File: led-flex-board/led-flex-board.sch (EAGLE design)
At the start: 30 parts

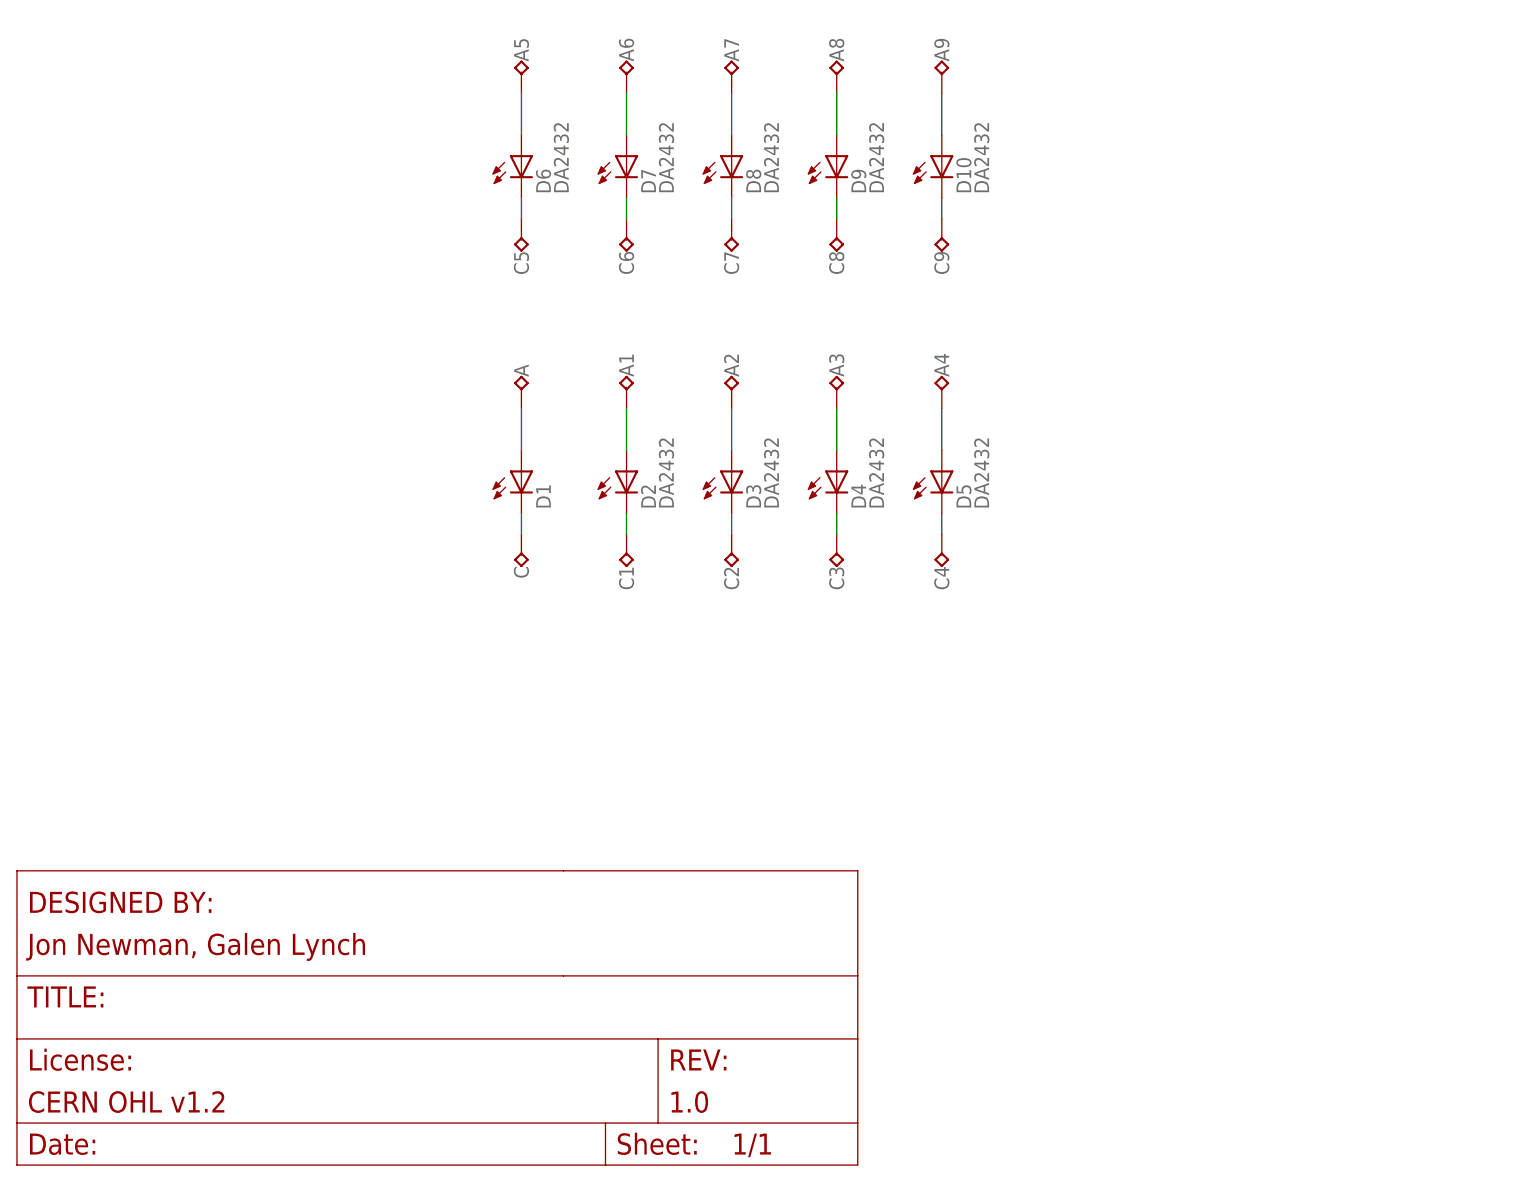
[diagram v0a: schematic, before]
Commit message: Added more designs to led-flex-board
- Multiple lead length options
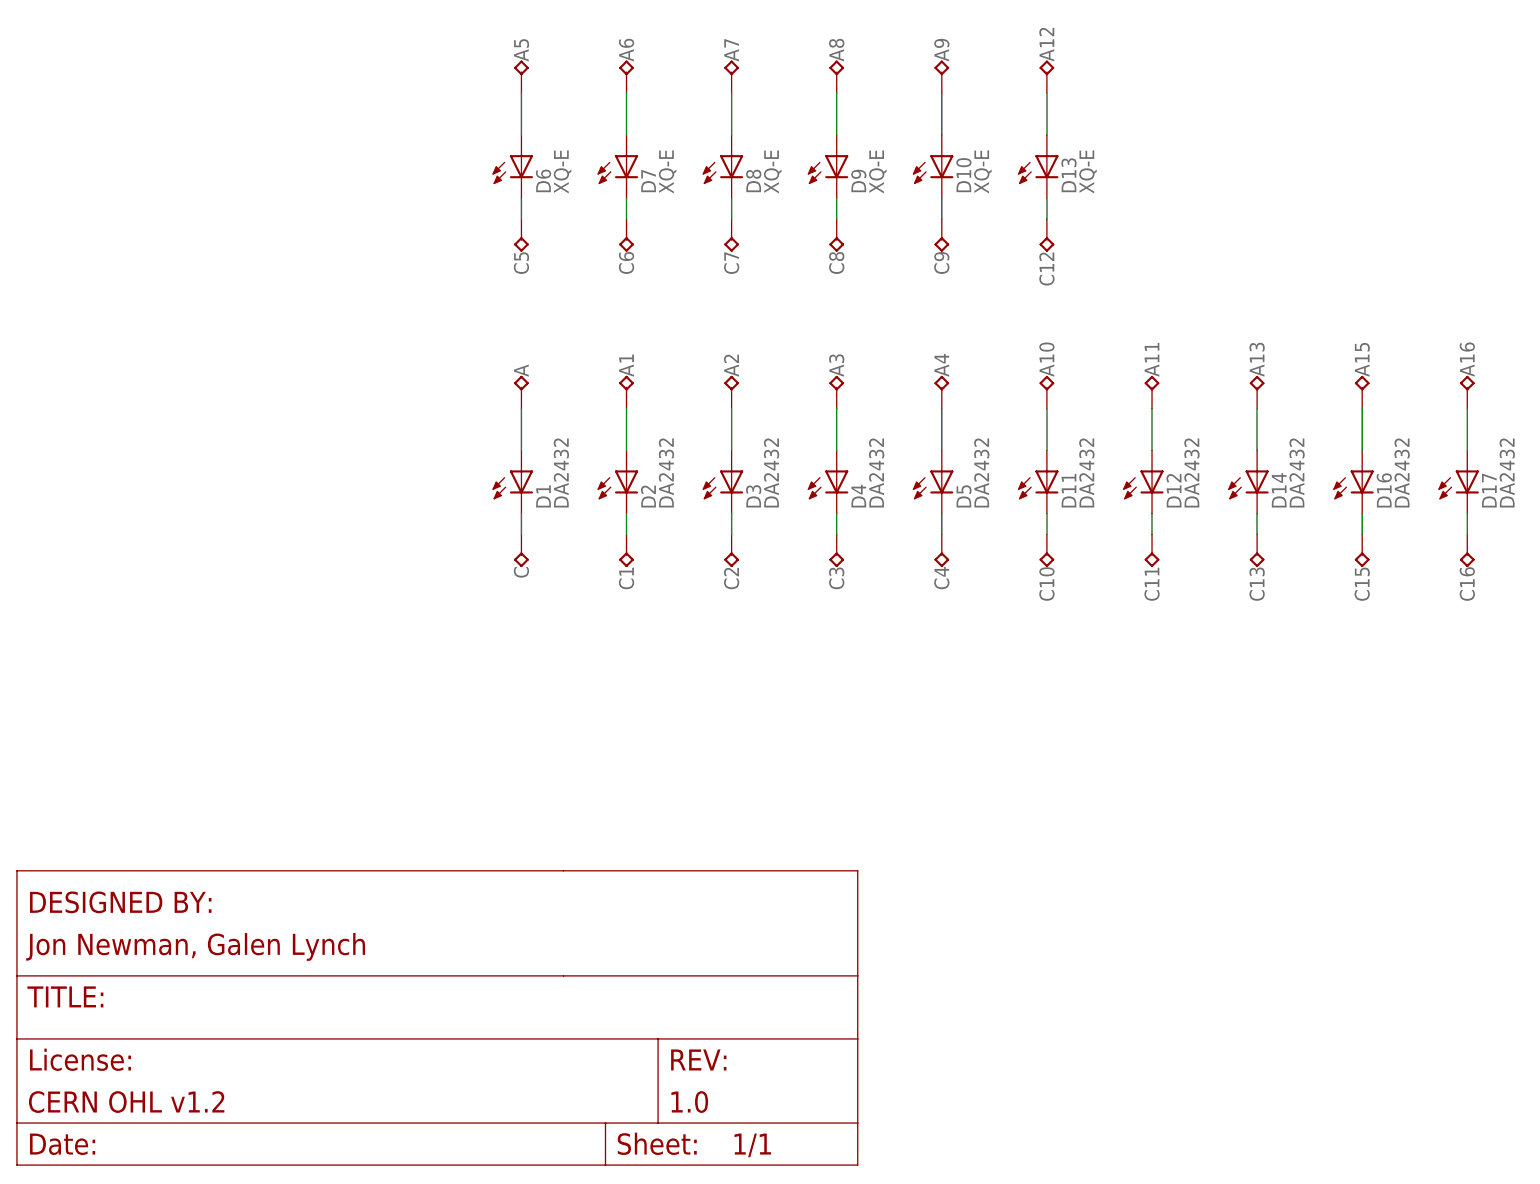
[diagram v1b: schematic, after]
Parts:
- added A10, A11, A12, A13, A15, A16, C10, C11, C12, C13, C15, C16: (no value), jonnew:TP_S0.6X1.5MM
- added D11, D12, D14, D16, D17: DA2432, jonnew:LED_DA2432
- added D13: XQ-E, jonnew:LED_XLAMP1.6X1.6MM
- D1: value (none) -> DA2432
- D10, D6, D7, D8, D9: value DA2432 -> XQ-E
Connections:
- new net N$21: C10.TP, D11.C
- new net N$22: A10.TP, D11.A
- new net N$23: C11.TP, D12.C
- new net N$24: A11.TP, D12.A
- new net N$25: C12.TP, D13.C
- new net N$26: A12.TP, D13.A
- new net N$27: C13.TP, D14.C
- new net N$28: A13.TP, D14.A
- new net N$31: C15.TP, D16.C
- new net N$32: A15.TP, D16.A
- new net N$33: C16.TP, D17.C
- new net N$34: A16.TP, D17.A
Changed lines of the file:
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@@
 </classes>
 <parts>
-<part name="D1" library="jonnew" deviceset="LED" device="_DA2432"/>
+<part name="D1" library="jonnew" deviceset="LED" device="_DA2432" value="DA2432"/>
 <part name="A" library="jonnew" deviceset="TP" device="_S0.6X1.5MM"/>
 <part name="C" library="jonnew" deviceset="TP" device="_S0.6X1.5MM"/>
@@
 <part name="A4" library="jonnew" deviceset="TP" device="_S0.6X1.5MM"/>
 <part name="C4" library="jonnew" deviceset="TP" device="_S0.6X1.5MM"/>
-<part name="D6" library="jonnew" deviceset="LED" device="_XLAMP1.6X1.6MM" value="DA2432"/>
+<part name="D6" library="jonnew" deviceset="LED" device="_XLAMP1.6X1.6MM" value="XQ-E"/>
 <part name="A5" library="jonnew" deviceset="TP" device="_S0.6X1.5MM"/>
 <part name="C5" library="jonnew" deviceset="TP" device="_S0.6X1.5MM"/>
-<part name="D7" library="jonnew" deviceset="LED" device="_XLAMP1.6X1.6MM" value="DA2432"/>
+<part name="D7" library="jonnew" deviceset="LED" device="_XLAMP1.6X1.6MM" value="XQ-E"/>
 <part name="A6" library="jonnew" deviceset="TP" device="_S0.6X1.5MM"/>
 <part name="C6" library="jonnew" deviceset="TP" device="_S0.6X1.5MM"/>
-<part name="D8" library="jonnew" deviceset="LED" device="_XLAMP1.6X1.6MM" value="DA2432"/>
+<part name="D8" library="jonnew" deviceset="LED" device="_XLAMP1.6X1.6MM" value="XQ-E"/>
 <part name="A7" library="jonnew" deviceset="TP" device="_S0.6X1.5MM"/>
 <part name="C7" library="jonnew" deviceset="TP" device="_S0.6X1.5MM"/>
-<part name="D9" library="jonnew" deviceset="LED" device="_XLAMP1.6X1.6MM" value="DA2432"/>
+<part name="D9" library="jonnew" deviceset="LED" device="_XLAMP1.6X1.6MM" value="XQ-E"/>
 <part name="A8" library="jonnew" deviceset="TP" device="_S0.6X1.5MM"/>
 <part name="C8" library="jonnew" deviceset="TP" device="_S0.6X1.5MM"/>
-<part name="D10" library="jonnew" deviceset="LED" device="_XLAMP1.6X1.6MM" value="DA2432"/>
+<part name="D10" library="jonnew" deviceset="LED" device="_XLAMP1.6X1.6MM" value="XQ-E"/>
 <part name="A9" library="jonnew" deviceset="TP" device="_S0.6X1.5MM"/>
 <part name="C9" library="jonnew" deviceset="TP" device="_S0.6X1.5MM"/>
 <part name="U$1" library="jonnew" deviceset="DOCFIELD-GEN" device=""/>
+<part name="D11" library="jonnew" deviceset="LED" device="_DA2432" value="DA2432"/>
+<part name="A10" library="jonnew" deviceset="TP" device="_S0.6X1.5MM"/>
+<part name="C10" library="jonnew" deviceset="TP" device="_S0.6X1.5MM"/>
+<part name="D12" library="jonnew" deviceset="LED" device="_DA2432" value="DA2432"/>
+<part name="A11" library="jonnew" deviceset="TP" device="_S0.6X1.5MM"/>
+<part name="C11" library="jonnew" deviceset="TP" device="_S0.6X1.5MM"/>
+<part name="D13" library="jonnew" deviceset="LED" device="_XLAMP1.6X1.6MM" value="XQ-E"/>
+<part name="A12" library="jonnew" deviceset="TP" device="_S0.6X1.5MM"/>
+<part name="C12" library="jonnew" deviceset="TP" device="_S0.6X1.5MM"/>
+<part name="D14" library="jonnew" deviceset="LED" device="_DA2432" value="DA2432"/>
+<part name="A13" library="jonnew" deviceset="TP" device="_S0.6X1.5MM"/>
+<part name="C13" library="jonnew" deviceset="TP" device="_S0.6X1.5MM"/>
+<part name="D16" library="jonnew" deviceset="LED" device="_DA2432" value="DA2432"/>
+<part name="A15" library="jonnew" deviceset="TP" device="_S0.6X1.5MM"/>
+<part name="C15" library="jonnew" deviceset="TP" device="_S0.6X1.5MM"/>
+<part name="D17" library="jonnew" deviceset="LED" device="_DA2432" value="DA2432"/>
+<part name="A16" library="jonnew" deviceset="TP" device="_S0.6X1.5MM"/>
+<part name="C16" library="jonnew" deviceset="TP" device="_S0.6X1.5MM"/>
 </parts>
 <sheets>
@@
 <instance part="C9" gate="G$1" x="121.92" y="119.38" rot="R180"/>
 <instance part="U$1" gate="G$1" x="10.16" y="7.62"/>
+<instance part="D11" gate="G$1" x="134.62" y="91.44"/>
+<instance part="A10" gate="G$1" x="134.62" y="101.6"/>
+<instance part="C10" gate="G$1" x="134.62" y="81.28" rot="R180"/>
+<instance part="D12" gate="G$1" x="147.32" y="91.44"/>
+<instance part="A11" gate="G$1" x="147.32" y="101.6"/>
+<instance part="C11" gate="G$1" x="147.32" y="81.28" rot="R180"/>
+<instance part="D13" gate="G$1" x="134.62" y="129.54"/>
+<instance part="A12" gate="G$1" x="134.62" y="139.7"/>
+<instance part="C12" gate="G$1" x="134.62" y="119.38" rot="R180"/>
+<instance part="D14" gate="G$1" x="160.02" y="91.44"/>
+<instance part="A13" gate="G$1" x="160.02" y="101.6"/>
+<instance part="C13" gate="G$1" x="160.02" y="81.28" rot="R180"/>
+<instance part="D16" gate="G$1" x="172.72" y="91.44"/>
+<instance part="A15" gate="G$1" x="172.72" y="101.6"/>
+<instance part="C15" gate="G$1" x="172.72" y="81.28" rot="R180"/>
+<instance part="D17" gate="G$1" x="185.42" y="91.44"/>
+<instance part="A16" gate="G$1" x="185.42" y="101.6"/>
+<instance part="C16" gate="G$1" x="185.42" y="81.28" rot="R180"/>
 </instances>
 <busses>
@@
 </segment>
 </net>
+<net name="N$21" class="0">
+<segment>
+<pinref part="C10" gate="G$1" pin="TP"/>
+<pinref part="D11" gate="G$1" pin="C"/>
+<wire x1="134.62" y1="83.82" x2="134.62" y2="86.36" width="0.1524" layer="91"/>
+</segment>
+</net>
+<net name="N$22" class="0">
+<segment>
+<pinref part="D11" gate="G$1" pin="A"/>
+<pinref part="A10" gate="G$1" pin="TP"/>
+<wire x1="134.62" y1="93.98" x2="134.62" y2="99.06" width="0.1524" layer="91"/>
+</segment>
+</net>
+<net name="N$23" class="0">
+<segment>
+<pinref part="C11" gate="G$1" pin="TP"/>
+<pinref part="D12" gate="G$1" pin="C"/>
+<wire x1="147.32" y1="83.82" x2="147.32" y2="86.36" width="0.1524" layer="91"/>
+</segment>
+</net>
+<net name="N$24" class="0">
+<segment>
+<pinref part="D12" gate="G$1" pin="A"/>
+<pinref part="A11" gate="G$1" pin="TP"/>
+<wire x1="147.32" y1="93.98" x2="147.32" y2="99.06" width="0.1524" layer="91"/>
+</segment>
+</net>
+<net name="N$25" class="0">
+<segment>
+<pinref part="C12" gate="G$1" pin="TP"/>
+<pinref part="D13" gate="G$1" pin="C"/>
+<wire x1="134.62" y1="121.92" x2="134.62" y2="124.46" width="0.1524" layer="91"/>
+</segment>
+</net>
+<net name="N$26" class="0">
+<segment>
+<pinref part="D13" gate="G$1" pin="A"/>
+<pinref part="A12" gate="G$1" pin="TP"/>
+<wire x1="134.62" y1="132.08" x2="134.62" y2="137.16" width="0.1524" layer="91"/>
+</segment>
+</net>
+<net name="N$27" class="0">
+<segment>
+<pinref part="C13" gate="G$1" pin="TP"/>
+<pinref part="D14" gate="G$1" pin="C"/>
+<wire x1="160.02" y1="83.82" x2="160.02" y2="86.36" width="0.1524" layer="91"/>
+</segment>
+</net>
+<net name="N$28" class="0">
+<segment>
+<pinref part="D14" gate="G$1" pin="A"/>
+<pinref part="A13" gate="G$1" pin="TP"/>
+<wire x1="160.02" y1="93.98" x2="160.02" y2="99.06" width="0.1524" layer="91"/>
+</segment>
+</net>
+<net name="N$31" class="0">
+<segment>
+<pinref part="C15" gate="G$1" pin="TP"/>
+<pinref part="D16" gate="G$1" pin="C"/>
+<wire x1="172.72" y1="83.82" x2="172.72" y2="86.36" width="0.1524" layer="91"/>
+</segment>
+</net>
+<net name="N$32" class="0">
+<segment>
+<pinref part="D16" gate="G$1" pin="A"/>
+<pinref part="A15" gate="G$1" pin="TP"/>
+<wire x1="172.72" y1="93.98" x2="172.72" y2="99.06" width="0.1524" layer="91"/>
+</segment>
+</net>
+<net name="N$33" class="0">
+<segment>
+<pinref part="C16" gate="G$1" pin="TP"/>
+<pinref part="D17" gate="G$1" pin="C"/>
+<wire x1="185.42" y1="83.82" x2="185.42" y2="86.36" width="0.1524" layer="91"/>
+</segment>
+</net>
+<net name="N$34" class="0">
+<segment>
+<pinref part="D17" gate="G$1" pin="A"/>
+<pinref part="A16" gate="G$1" pin="TP"/>
+<wire x1="185.42" y1="93.98" x2="185.42" y2="99.06" width="0.1524" layer="91"/>
+</segment>
+</net>
